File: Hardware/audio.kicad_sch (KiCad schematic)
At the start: 16 parts, among them J8 Conn_01x03, U4 LP5907MFX-3.3, U5 PCM5100

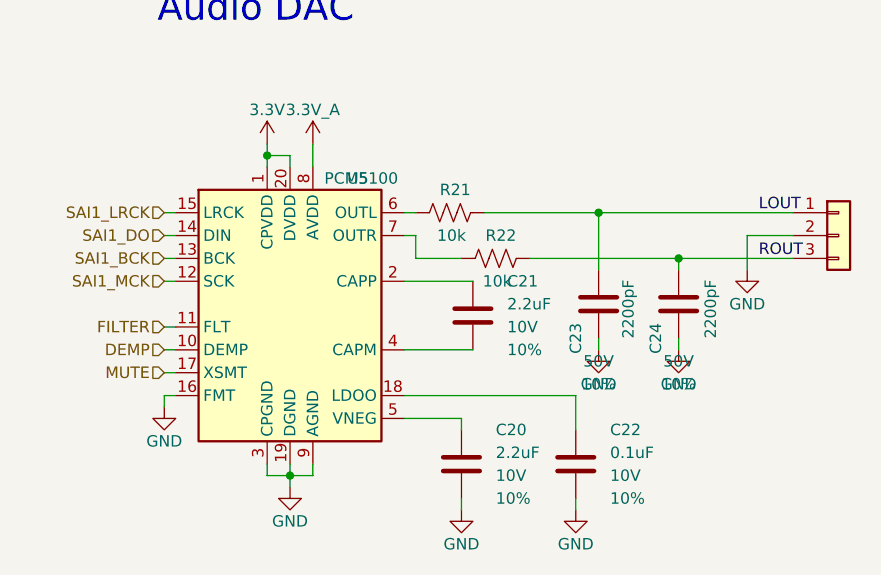
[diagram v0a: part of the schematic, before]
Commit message: Reduced board length by 0.25" and completed initial component placement. Added 3D models.
Signed-off-by: Jamie Robertson <jrr@robertsonics.com>
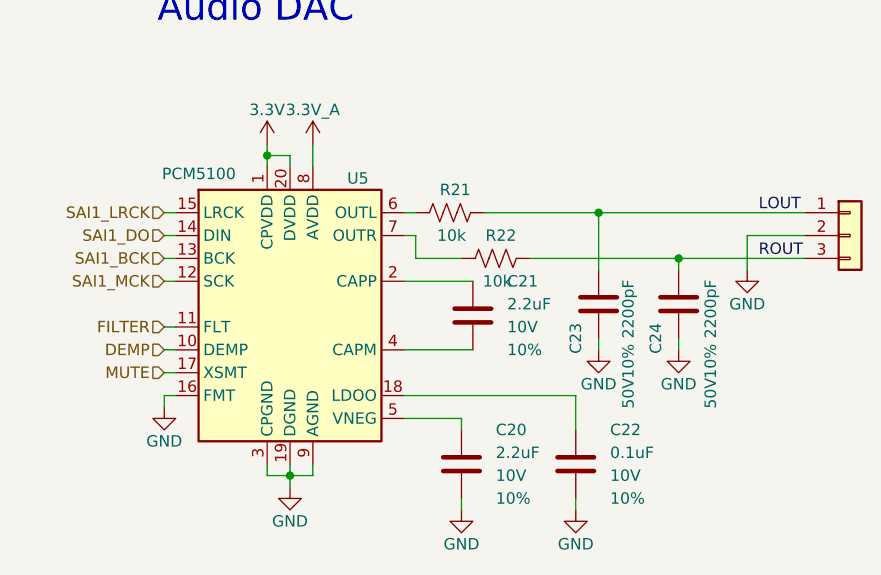
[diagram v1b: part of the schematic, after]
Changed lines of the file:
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@@
 	(wire
 		(pts
-			(xy 234.95 85.09) (xy 256.54 85.09)
+			(xy 234.95 85.09) (xy 257.81 85.09)
 		)
 		(stroke
@@
 	(wire
 		(pts
-			(xy 243.84 90.17) (xy 256.54 90.17)
+			(xy 243.84 90.17) (xy 257.81 90.17)
 		)
 		(stroke
@@
 	(wire
 		(pts
-			(xy 256.54 87.63) (xy 251.46 87.63)
+			(xy 257.81 87.63) (xy 251.46 87.63)
 		)
 		(stroke
@@
 		)
 		(property "Voltage" "50V"
-			(at 243.84 101.6 0)
+			(at 247.396 105.156 90)
 			(effects
 				(font
@@
 		)
 		(property "Tolerance" "10%"
-			(at 243.84 104.14 0)
+			(at 247.396 101.6 90)
 			(effects
 				(font
@@
 	(symbol
 		(lib_id "SparkFun-Connector:Conn_01x03")
-		(at 261.62 87.63 0)
+		(at 262.89 87.63 0)
 		(unit 1)
 		(exclude_from_sim no)
@@
 		(fields_autoplaced yes)
 		(property "Reference" "J8"
-			(at 261.62 82.55 0)
+			(at 262.89 82.55 0)
 			(effects
 				(font
@@
 		)
 		(property "Value" "Conn_01x03"
-			(at 261.62 92.71 0)
+			(at 262.89 92.71 0)
 			(effects
 				(font
@@
 		)
 		(property "Footprint" "SparkFun-Connector:1x03"
-			(at 261.62 95.25 0)
+			(at 262.89 95.25 0)
 			(effects
 				(font
@@
 		)
 		(property "Datasheet" "~"
-			(at 261.62 96.52 0)
+			(at 262.89 96.52 0)
 			(effects
 				(font
@@
 		)
 		(property "Description" ""
-			(at 261.62 87.63 0)
+			(at 262.89 87.63 0)
 			(effects
 				(font
@@
 		)
 		(property "Voltage" "50V"
-			(at 234.95 101.6 0)
+			(at 238.252 105.156 90)
 			(effects
 				(font
@@
 		)
 		(property "Tolerance" "10%"
-			(at 234.95 104.14 0)
+			(at 238.252 101.6 90)
 			(effects
 				(font
@@
 		)
 		(property "Value" "PCM5100"
-			(at 204.47 81.28 0)
+			(at 186.436 80.772 0)
 			(effects
 				(font

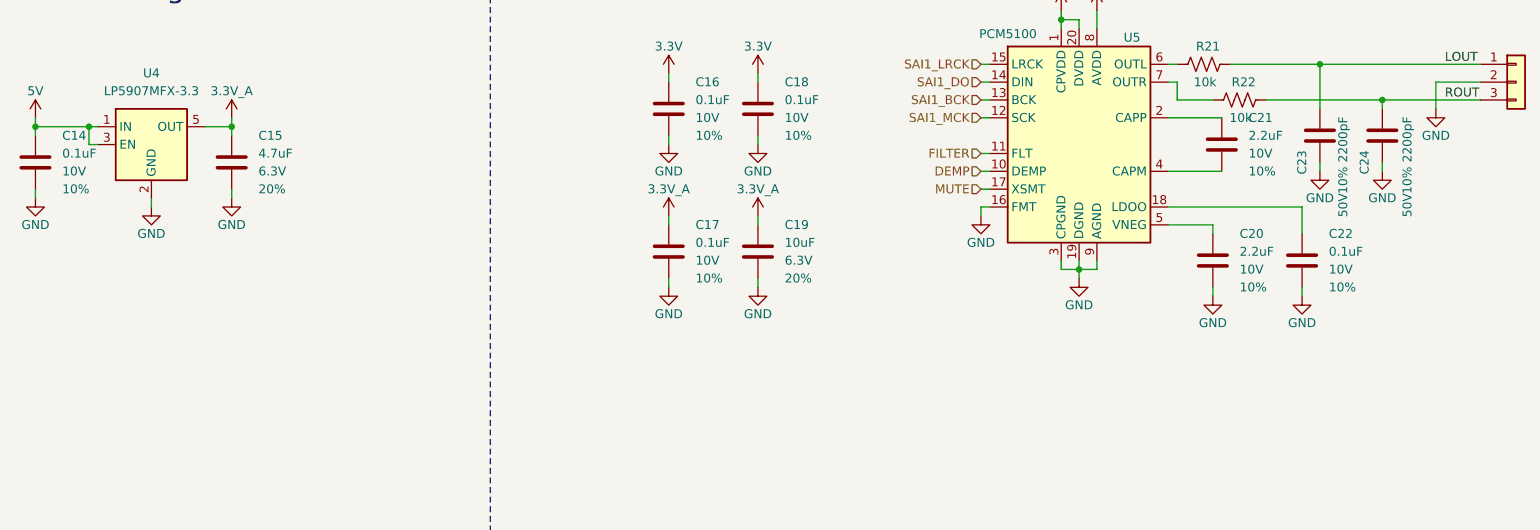
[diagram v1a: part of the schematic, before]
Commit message: Finished first pass routing entire board.
Signed-off-by: Jamie Robertson <jrr@robertsonics.com>
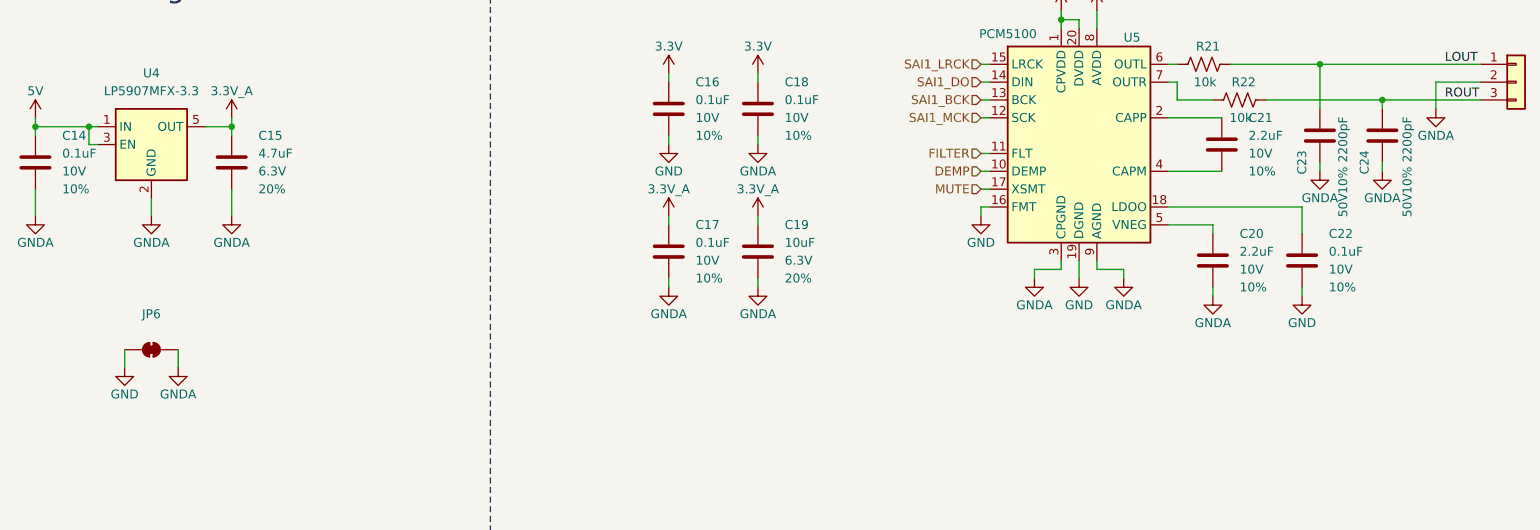
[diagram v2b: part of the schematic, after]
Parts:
- added JP6: ~, SparkFun-Jumper:Jumper_2_NC_Trace, symbol SparkFun-Jumper:SolderJumper_2_Bridged
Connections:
- net GND: now also JP6.2 (B); no longer C14.2, C15.2, C17.2, C18.2, C19.2, C20.2, C23.2, C24.2, J8.2 (Pin_2), U4.2 (GND), U5.3 (CPGND), U5.9 (AGND)
- new net GNDA: C14.2, C15.2, C17.2, C18.2, C19.2, C20.2, C23.2, C24.2, J8.2 (Pin_2), JP6.1 (A), U4.2 (GND), U5.3 (CPGND), U5.9 (AGND)

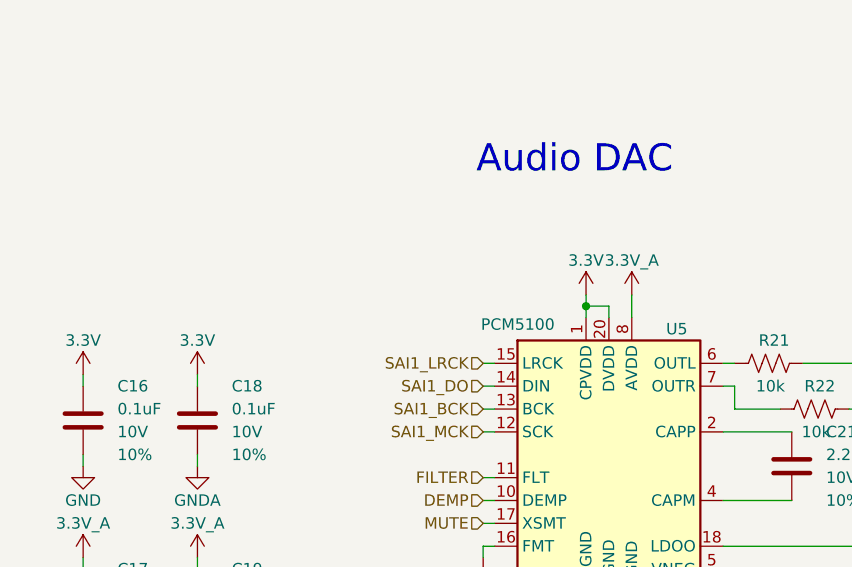
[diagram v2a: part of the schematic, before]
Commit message: Finished labels. Fixed DRC errors.
Signed-off-by: Jamie Robertson <jrr@robertsonics.com>
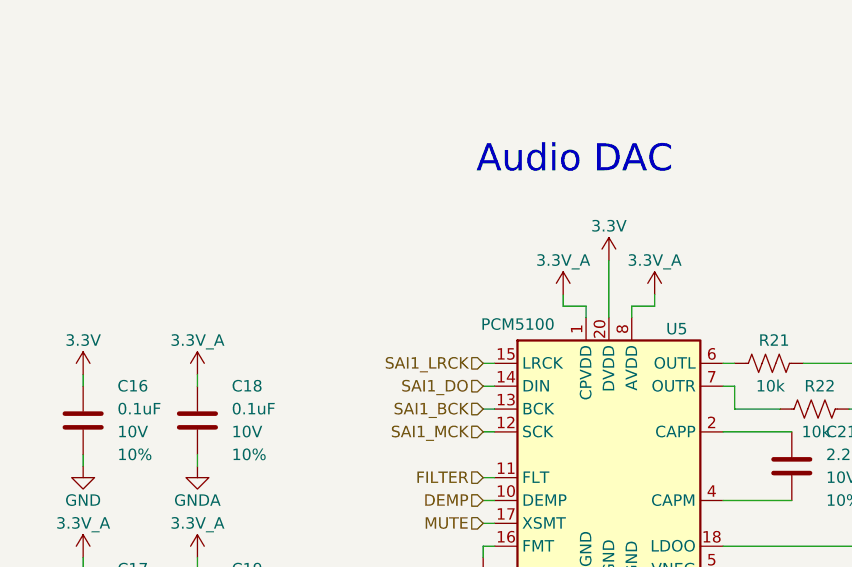
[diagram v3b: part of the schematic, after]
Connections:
- net 3.3V: no longer C18.1, U5.1 (CPVDD)
- net 3.3V_A: now also C18.1, U5.1 (CPVDD)
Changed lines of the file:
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@@
 	)
 	(junction
-		(at 198.12 78.74)
-		(diameter 0)
-		(color 0 0 0 0)
-	)
-	(junction
 		(at 52.07 93.98)
 		(diameter 0)
@@
 	(wire
 		(pts
-			(xy 203.2 77.47) (xy 203.2 80.01)
-		)
-		(stroke
-			(width 0)
-			(type default)
-		)
-	)
-	(wire
-		(pts
 			(xy 213.36 105.41) (xy 232.41 105.41)
 		)
@@
 	(wire
 		(pts
+			(xy 198.12 78.74) (xy 195.58 78.74)
+		)
+		(stroke
+			(width 0)
+			(type default)
+		)
+	)
+	(wire
+		(pts
 			(xy 214.63 85.09) (xy 213.36 85.09)
 		)
@@
 	(wire
 		(pts
-			(xy 198.12 78.74) (xy 200.66 78.74)
+			(xy 205.74 78.74) (xy 205.74 77.47)
 		)
 		(stroke
@@
 	(wire
 		(pts
+			(xy 198.12 80.01) (xy 198.12 78.74)
+		)
+		(stroke
+			(width 0)
+			(type default)
+		)
+	)
+	(wire
+		(pts
 			(xy 203.2 114.3) (xy 207.01 114.3)
 		)
@@
 	(wire
 		(pts
-			(xy 200.66 78.74) (xy 200.66 80.01)
+			(xy 200.66 73.66) (xy 200.66 80.01)
 		)
 		(stroke
@@
 	(wire
 		(pts
+			(xy 195.58 78.74) (xy 195.58 77.47)
+		)
+		(stroke
+			(width 0)
+			(type default)
+		)
+	)
+	(wire
+		(pts
 			(xy 198.12 114.3) (xy 194.31 114.3)
 		)
@@
 	(wire
 		(pts
-			(xy 198.12 78.74) (xy 198.12 80.01)
+			(xy 142.24 96.52) (xy 142.24 95.25)
 		)
 		(stroke
@@
 	(wire
 		(pts
-			(xy 142.24 96.52) (xy 142.24 95.25)
+			(xy 142.24 107.95) (xy 142.24 106.68)
 		)
 		(stroke
@@
 	(wire
 		(pts
-			(xy 142.24 107.95) (xy 142.24 106.68)
+			(xy 80.01 93.98) (xy 80.01 95.25)
 		)
 		(stroke
@@
 	(wire
 		(pts
-			(xy 80.01 93.98) (xy 80.01 95.25)
+			(xy 203.2 80.01) (xy 203.2 78.74)
 		)
 		(stroke
@@
 	(wire
 		(pts
-			(xy 198.12 77.47) (xy 198.12 78.74)
+			(xy 52.07 93.98) (xy 52.07 95.25)
 		)
 		(stroke
@@
 	(wire
 		(pts
-			(xy 52.07 93.98) (xy 52.07 95.25)
+			(xy 200.66 113.03) (xy 200.66 115.57)
 		)
 		(stroke
@@
 	(wire
 		(pts
-			(xy 200.66 113.03) (xy 200.66 115.57)
+			(xy 203.2 78.74) (xy 205.74 78.74)
 		)
 		(stroke
@@
 	)
 	(symbol
-		(lib_id "SparkFun-PowerSymbol:3.3V")
-		(at 154.94 86.36 0)
-		(unit 1)
-		(exclude_from_sim no)
-		(in_bom yes)
-		(on_board yes)
-		(dnp no)
-		(fields_autoplaced yes)
-		(property "Reference" "#PWR061"
-			(at 154.94 90.17 0)
-			(effects
-				(font
-					(size 1.27 1.27)
-				)
-				(hide yes)
-			)
-		)
-		(property "Value" "3.3V"
-			(at 154.94 82.55 0)
-			(do_not_autoplace yes)
-			(effects
-				(font
-					(size 1.27 1.27)
-				)
-			)
-		)
-		(property "Footprint" ""
-			(at 154.94 86.36 0)
-			(effects
-				(font
-					(size 1.27 1.27)
-				)
-				(hide yes)
-			)
-		)
-		(property "Datasheet" ""
-			(at 154.94 86.36 0)
-			(effects
-				(font
-					(size 1.27 1.27)
-				)
-				(hide yes)
-			)
-		)
-		(property "Description" ""
-			(at 154.94 86.36 0)
-			(effects
-				(font
-					(size 1.27 1.27)
-				)
-				(hide yes)
-			)
-		)
-		(pin "1"
-		)
-		(instances
-			(project "SparkFun_Qwiic_Turntable"
-				(path "/4c0b78e3-6801-43aa-85ca-70880324c2bd/79c75e5e-ffba-407e-9374-79e1c26e51a6"
-					(reference "#PWR061")
-					(unit 1)
-				)
-			)
-		)
-	)
-	(symbol
 		(lib_id "SparkFun-Capacitor:0.1uF_0402_10V_10%")
 		(at 232.41 113.03 0)
@@
 	(symbol
 		(lib_id "SparkFun-PowerSymbol:3.3V_A")
-		(at 203.2 77.47 0)
+		(at 205.74 77.47 0)
 		(unit 1)
 		(exclude_from_sim no)
@@
 		(fields_autoplaced yes)
 		(property "Reference" "#PWR068"
-			(at 203.2 81.28 0)
+			(at 205.74 81.28 0)
 			(effects
 				(font
@@
 		)
 		(property "Value" "3.3V_A"
-			(at 203.2 73.66 0)
+			(at 205.74 73.66 0)
 			(do_not_autoplace yes)
 			(effects
@@
 		)
 		(property "Footprint" ""
-			(at 203.2 77.47 0)
+			(at 205.74 77.47 0)
 			(effects
 				(font
@@
 		)
 		(property "Datasheet" ""
-			(at 203.2 77.47 0)
+			(at 205.74 77.47 0)
 			(effects
 				(font
@@
 		)
 		(property "Description" ""
-			(at 203.2 77.47 0)
+			(at 205.74 77.47 0)
 			(effects
 				(font
@@
 	)
 	(symbol
+		(lib_id "SparkFun-PowerSymbol:3.3V_A")
+		(at 195.58 77.47 0)
+		(unit 1)
+		(exclude_from_sim no)
+		(in_bom yes)
+		(on_board yes)
+		(dnp no)
+		(fields_autoplaced yes)
+		(property "Reference" "#PWR081"
+			(at 195.58 81.28 0)
+			(effects
+				(font
+					(size 1.27 1.27)
+				)
+				(hide yes)
+			)
+		)
+		(property "Value" "3.3V_A"
+			(at 195.58 73.66 0)
+			(do_not_autoplace yes)
+			(effects
+				(font
+					(size 1.27 1.27)
+				)
+			)
+		)
+		(property "Footprint" ""
+			(at 195.58 77.47 0)
+			(effects
+				(font
+					(size 1.27 1.27)
+				)
+				(hide yes)
+			)
+		)
+		(property "Datasheet" ""
+			(at 195.58 77.47 0)
+			(effects
+				(font
+					(size 1.27 1.27)
+				)
+				(hide yes)
+			)
+		)
+		(property "Description" ""
+			(at 195.58 77.47 0)
+			(effects
+				(font
+					(size 1.27 1.27)
+				)
+				(hide yes)
+			)
+		)
+		(pin "1"
+		)
+		(instances
+			(project "SparkFun_Qwiic_Turntable"
+				(path "/4c0b78e3-6801-43aa-85ca-70880324c2bd/79c75e5e-ffba-407e-9374-79e1c26e51a6"
+					(reference "#PWR081")
+					(unit 1)
+				)
+			)
+		)
+	)
+	(symbol
 		(lib_id "SparkFun-Connector:Conn_01x03")
 		(at 262.89 87.63 0)
@@
 	)
 	(symbol
+		(lib_id "SparkFun-PowerSymbol:3.3V_A")
+		(at 154.94 86.36 0)
+		(unit 1)
+		(exclude_from_sim no)
+		(in_bom yes)
+		(on_board yes)
+		(dnp no)
+		(fields_autoplaced yes)
+		(property "Reference" "#PWR061"
+			(at 154.94 90.17 0)
+			(effects
+				(font
+					(size 1.27 1.27)
+				)
+				(hide yes)
+			)
+		)
+		(property "Value" "3.3V_A"
+			(at 154.94 82.55 0)
+			(do_not_autoplace yes)
+			(effects
+				(font
+					(size 1.27 1.27)
+				)
+			)
+		)
+		(property "Footprint" ""
+			(at 154.94 86.36 0)
+			(effects
+				(font
+					(size 1.27 1.27)
+				)
+				(hide yes)
+			)
+		)
+		(property "Datasheet" ""
+			(at 154.94 86.36 0)
+			(effects
+				(font
+					(size 1.27 1.27)
+				)
+				(hide yes)
+			)
+		)
+		(property "Description" ""
+			(at 154.94 86.36 0)
+			(effects
+				(font
+					(size 1.27 1.27)
+				)
+				(hide yes)
+			)
+		)
+		(pin "1"
+		)
+		(instances
+			(project "SparkFun_Qwiic_Turntable"
+				(path "/4c0b78e3-6801-43aa-85ca-70880324c2bd/79c75e5e-ffba-407e-9374-79e1c26e51a6"
+					(reference "#PWR061")
+					(unit 1)
+				)
+			)
+		)
+	)
+	(symbol
 		(lib_id "SparkFun-PowerSymbol:5V")
 		(at 52.07 92.71 0)
@@
 	(symbol
 		(lib_id "SparkFun-PowerSymbol:3.3V")
-		(at 198.12 77.47 0)
+		(at 200.66 73.66 0)
 		(unit 1)
 		(exclude_from_sim no)
@@
 		(fields_autoplaced yes)
 		(property "Reference" "#PWR066"
-			(at 198.12 81.28 0)
+			(at 200.66 77.47 0)
 			(effects
 				(font
@@
 		)
 		(property "Value" "3.3V"
-			(at 198.12 73.66 0)
+			(at 200.66 69.85 0)
 			(do_not_autoplace yes)
 			(effects
@@
 		)
 		(property "Footprint" ""
-			(at 198.12 77.47 0)
+			(at 200.66 73.66 0)
 			(effects
 				(font
@@
 		)
 		(property "Datasheet" ""
-			(at 198.12 77.47 0)
+			(at 200.66 73.66 0)
 			(effects
 				(font
@@
 		)
 		(property "Description" ""
-			(at 198.12 77.47 0)
+			(at 200.66 73.66 0)
 			(effects
 				(font
